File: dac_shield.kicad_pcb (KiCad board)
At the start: 2 copper layers, 68.6 x 53.3 mm, 32 parts, among them P1 V+, P2 GND, P3 V-, P4 Out, P5 GND, U1 LM741, U2 TCA0372

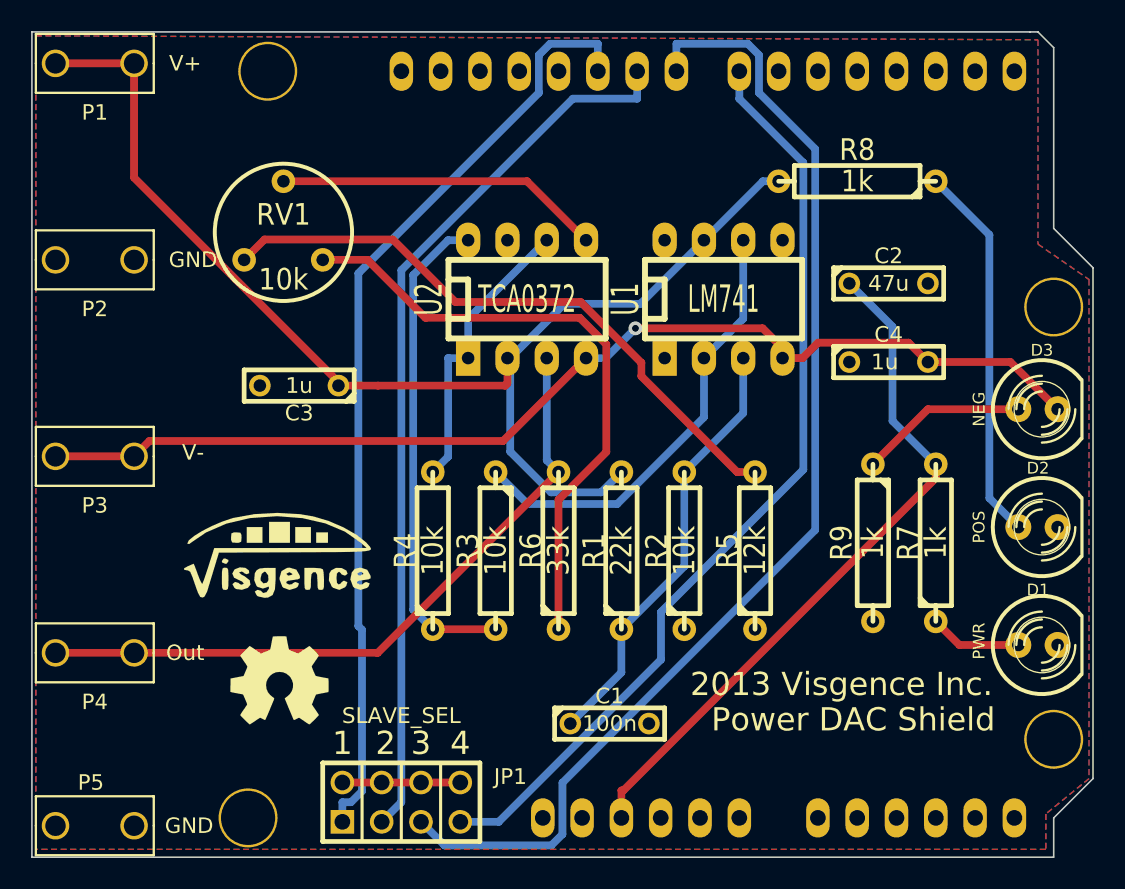
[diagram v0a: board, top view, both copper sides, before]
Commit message: Added DAC back on board
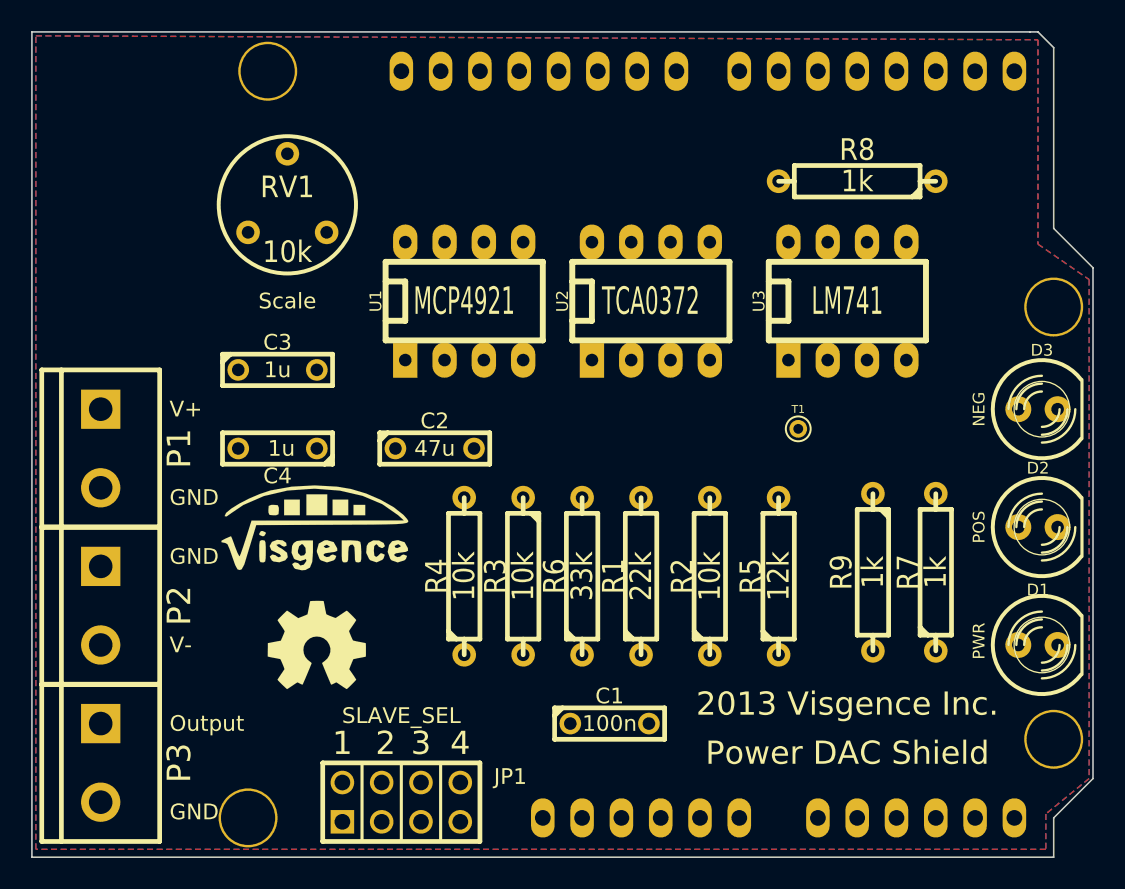
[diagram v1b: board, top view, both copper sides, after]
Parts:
- removed P4: Out, Johnson_Banana
- removed P5: GND, Johnson_Banana
- added T1: VrefTest, PINTST, F.Cu at (80.0, 54.6)
- added U3: LM741, DIP-8__300_ELL, F.Cu at (83.2, 46.4)
- P1: value V+ -> CONN_2; footprint Johnson_Banana -> bornier2
- P2: value GND -> CONN_2; footprint Johnson_Banana -> bornier2
- P3: value V- -> CONN_2; footprint Johnson_Banana -> bornier2
- U1: value LM741 -> MCP4921
- moved C4 39.9 mm to (46.4, 55.9), turned to 180 degrees
- moved C2 31.2 mm to (56.5, 55.9)
- moved P1 24.9 mm to (34.9, 55.9), turned to 270 degrees
- moved P2 22.4 mm to (34.9, 66.0), turned to 270 degrees
- moved P3 19.8 mm to (34.9, 76.2), turned to 270 degrees
- moved U1 16.8 mm to (58.4, 46.4)
- moved U2 8.00 mm to (70.5, 46.4)
- moved G2 3.32 mm to (48.9, 68.6)
- moved G1 3.00 mm to (48.9, 61.0)
- moved R4 2.62 mm to (58.4, 64.1)
- moved R3 2.43 mm to (62.2, 64.1)
- moved R2 2.33 mm to (74.3, 64.1)
- moved R5 2.25 mm to (78.7, 64.1)
- moved R6 2.25 mm to (66.0, 64.1)
- moved R1 2.08 mm to (69.8, 64.1)
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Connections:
- C1 pad 1: N-000005 (its old number) -> N-000007
- JP1 pad 2: N-000032 -> N-000037
- JP1 pad 4: N-000032 -> N-000037
- JP1 pad 6: N-000032 -> N-000037
- JP1 pad 8: N-000032 -> N-000037
- P3 pad 1: VSS -> N-000009
- R1 pad 1: N-000005 (its old number) -> N-000007
- R2 pad 2: N-000005 (its old number) -> N-000007
- R6 pad 2: N-000008 -> N-000009
- U1 pad 1: (no net) -> +5V
- U1 pad 2: VREF -> N-000037
- U1 pad 3: N-000005 (its old number) -> CLK
- U1 pad 4: VSS -> MOSI
- U1 pad 5: (no net) -> GND
- U1 pad 7: VDD -> GND
- U1 pad 8: (no net) -> DAC_OUT
- U2 pad 3: N-000008 -> N-000009
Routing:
- net VDD: track 81.0 -> 0.00 mm
- net N-000035: track 76.1 -> 0.00 mm
- net VSS: track 71.8 -> 0.00 mm, vias 1 -> 0
- net N-000036: track 61.2 -> 0.00 mm
- net N-000034: track 60.9 -> 0.00 mm
- net N-000033: track 57.8 -> 0.00 mm
- net +5V: track 45.4 -> 0.00 mm
- net N-000008: track 45.0 -> 0.00 mm
- net N-000039: track 40.3 -> 0.00 mm
- net N-000040: track 40.3 -> 0.00 mm
- net N-000041: track 32.0 -> 0.00 mm
- net VREF: track 29.1 -> 0.00 mm
- net N-000005 (its old number): track 28.3 -> 0.00 mm
- net N-000003: track 24.6 -> 0.00 mm
- net N-000043: track 21.1 -> 0.00 mm
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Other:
- board text added: "GND"
- board text added: "Output"
- board text added: "Scale"
- board text added: "V+"
- board text added: "V-"

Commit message: Added pinouts on silk screen
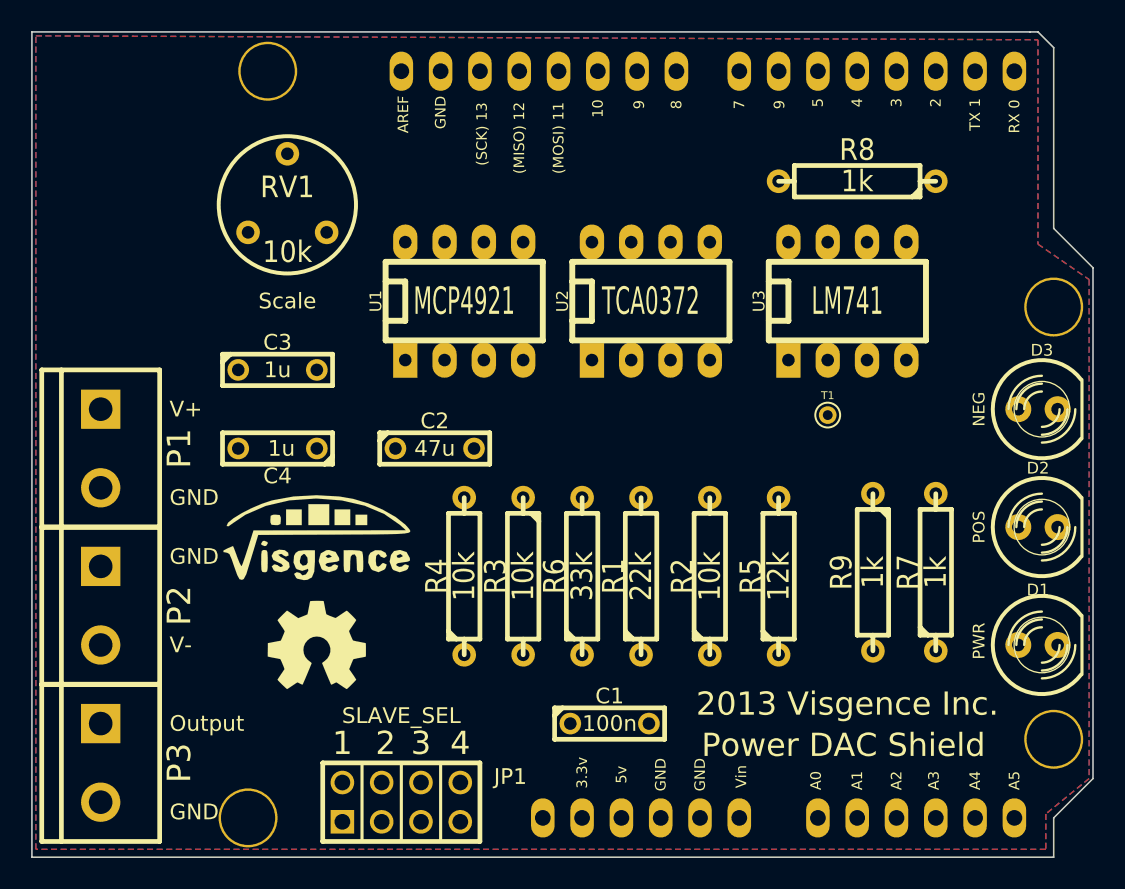
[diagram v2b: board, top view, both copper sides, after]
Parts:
- moved T1 2.10 mm to (81.9, 53.7)
- moved G1 0.65 mm to (49.0, 61.6)
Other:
- board text added: "(MISO) 12"
- board text added: "(MOSI) 11"
- board text added: "(SCK) 13"
- board text added: "10"
- board text added: "3.3v"
- board text added: "5"
- board text added: "5v"
- board text added: "6"
- board text added: "7"
- board text added: "8"
- board text added: "9"
- board text added: "A0"
- board text added: "A1"
- board text added: "A2"
- board text added: "A3"
- board text added: "A4"
- board text added: "A5"
- board text added: "AREF"
- board text added: "RX 0"
- board text added: "TX 1"
- board text added: "Vin"
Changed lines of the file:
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@@
     (area 30.429999 28.905999 99.110001 82.346001)
     (thickness 1.6)
-    (drawings 26)
+    (drawings 53)
     (tracks 0)
     (zones 0)
@@
     (trace_min 0.254)
     (segment_width 0.2)
-    (edge_width 0.1)
+    (edge_width 0.127)
     (via_size 0.889)
     (via_drill 0.635)
@@
     (uvia_min_size 0.508)
     (uvia_min_drill 0.127)
-    (pcb_text_width 0.3)
-    (pcb_text_size 1.016 1.016)
+    (pcb_text_width 0.127)
+    (pcb_text_size 0.6858 0.6858)
     (mod_edge_width 0.15)
     (mod_text_size 1 1)
@@
   )
   (module LOGO (layer F.Cu)
-    (at 48.895 60.96)
+    (at 49.022 61.595)
     (fp_text reference G1 (at 0 3.63982) (layer F.SilkS) hide
       (effects (font (size 1.524 1.524) (thickness 0.3048)))
@@
   )
   (module PINTST (layer F.Cu)
-    (at 80.01 54.61)
+    (at 81.915 53.721)
     (descr "module 1 pin (ou trou mecanique de percage)")
     (tags DEV)
@@
     )
   )
+  (gr_text A5 (at 93.98 77.343 90) (layer F.SilkS)
+    (effects (font (size 0.6858 0.6858) (thickness 0.127)))
+  )
+  (gr_text A4 (at 91.44 77.343 90) (layer F.SilkS)
+    (effects (font (size 0.6858 0.6858) (thickness 0.127)))
+  )
+  (gr_text A3 (at 88.773 77.343 90) (layer F.SilkS)
+    (effects (font (size 0.6858 0.6858) (thickness 0.127)))
+  )
+  (gr_text A2 (at 86.36 77.343 90) (layer F.SilkS)
+    (effects (font (size 0.6858 0.6858) (thickness 0.127)))
+  )
+  (gr_text A1 (at 83.82 77.343 90) (layer F.SilkS)
+    (effects (font (size 0.6858 0.6858) (thickness 0.127)))
+  )
+  (gr_text A0 (at 81.153 77.343 90) (layer F.SilkS)
+    (effects (font (size 0.6858 0.6858) (thickness 0.127)))
+  )
+  (gr_text Vin (at 76.327 77.089 90) (layer F.SilkS)
+    (effects (font (size 0.6858 0.6858) (thickness 0.127)))
+  )
+  (gr_text GND (at 73.66 76.962 90) (layer F.SilkS)
+    (effects (font (size 0.6858 0.6858) (thickness 0.127)))
+  )
+  (gr_text GND (at 71.12 76.962 90) (layer F.SilkS)
+    (effects (font (size 0.6858 0.6858) (thickness 0.127)))
+  )
+  (gr_text 5v (at 68.58 76.962 90) (layer F.SilkS)
+    (effects (font (size 0.6858 0.6858) (thickness 0.127)))
+  )
+  (gr_text 3.3v (at 66.04 76.835 90) (layer F.SilkS)
+    (effects (font (size 0.6858 0.6858) (thickness 0.127)))
+  )
+  (gr_text "RX 0" (at 93.98 34.417 90) (layer F.SilkS)
+    (effects (font (size 0.6858 0.6858) (thickness 0.127)))
+  )
+  (gr_text "TX 1" (at 91.44 34.29 90) (layer F.SilkS)
+    (effects (font (size 0.6858 0.6858) (thickness 0.127)))
+  )
+  (gr_text 2 (at 88.9 33.528 90) (layer F.SilkS)
+    (effects (font (size 0.6858 0.6858) (thickness 0.127)))
+  )
+  (gr_text 3 (at 86.36 33.528 90) (layer F.SilkS)
+    (effects (font (size 0.6858 0.6858) (thickness 0.127)))
+  )
+  (gr_text 4 (at 83.82 33.528 90) (layer F.SilkS)
+    (effects (font (size 0.6858 0.6858) (thickness 0.127)))
+  )
+  (gr_text 5 (at 81.28 33.528 90) (layer F.SilkS)
+    (effects (font (size 0.6858 0.6858) (thickness 0.127)))
+  )
+  (gr_text 6 (at 78.74 33.655 270) (layer F.SilkS)
+    (effects (font (size 0.6858 0.6858) (thickness 0.127)))
+  )
+  (gr_text 7 (at 76.2 33.655 90) (layer F.SilkS)
+    (effects (font (size 0.6858 0.6858) (thickness 0.127)))
+  )
+  (gr_text 8 (at 72.136 33.655 90) (layer F.SilkS)
+    (effects (font (size 0.6858 0.6858) (thickness 0.127)))
+  )
+  (gr_text 9 (at 69.723 33.655 90) (layer F.SilkS)
+    (effects (font (size 0.6858 0.6858) (thickness 0.127)))
+  )
+  (gr_text 10 (at 67.056 33.909 90) (layer F.SilkS)
+    (effects (font (size 0.6858 0.6858) (thickness 0.127)))
+  )
+  (gr_text "(MOSI) 11" (at 64.516 35.814 90) (layer F.SilkS)
+    (effects (font (size 0.6858 0.6858) (thickness 0.127)))
+  )
+  (gr_text "(MISO) 12" (at 61.976 35.814 90) (layer F.SilkS)
+    (effects (font (size 0.6858 0.6858) (thickness 0.127)))
+  )
+  (gr_text "(SCK) 13" (at 59.563 35.56 90) (layer F.SilkS)
+    (effects (font (size 0.6858 0.6858) (thickness 0.127)))
+  )
+  (gr_text AREF (at 54.483 34.29 90) (layer F.SilkS)
+    (effects (font (size 0.6858 0.6858) (thickness 0.127)))
+  )
+  (gr_text GND (at 56.896 34.163 90) (layer F.SilkS)
+    (effects (font (size 0.6858 0.6858) (thickness 0.127)))
+  )
   (gr_text Scale (at 46.99 46.355) (layer F.SilkS)
     (effects (font (size 1.016 1.016) (thickness 0.254)))
@@
     (effects (font (size 1.5 1.5) (thickness 0.3)))
   )
-  (gr_text "Power DAC Shield" (at 83.185 75.565) (layer F.SilkS)
+  (gr_text "Power DAC Shield" (at 82.931 75.057) (layer F.SilkS)
     (effects (font (size 1.5 1.5) (thickness 0.3)))
   )

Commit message: Did first try at routing
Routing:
- net N-000035: track 0.00 -> 93.6 mm
- net N-000034: track 0.00 -> 92.1 mm
- net VSS: track 0.00 -> 74.6 mm
- net VDD: track 0.00 -> 66.6 mm
- net N-000036: track 0.00 -> 65.1 mm
- net N-000040: track 0.00 -> 64.4 mm
- net +5V: track 0.00 -> 63.0 mm
- net N-000033: track 0.00 -> 61.0 mm, vias 0 -> 1
- net N-000009: track 0.00 -> 52.8 mm
- net VREF: track 0.00 -> 49.7 mm, vias 0 -> 1
- net N-000039: track 0.00 -> 45.3 mm
- net N-000037: track 0.00 -> 34.8 mm
- net N-000007: track 0.00 -> 33.8 mm
- net N-000041: track 0.00 -> 32.3 mm
- net N-000043: track 0.00 -> 29.7 mm
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
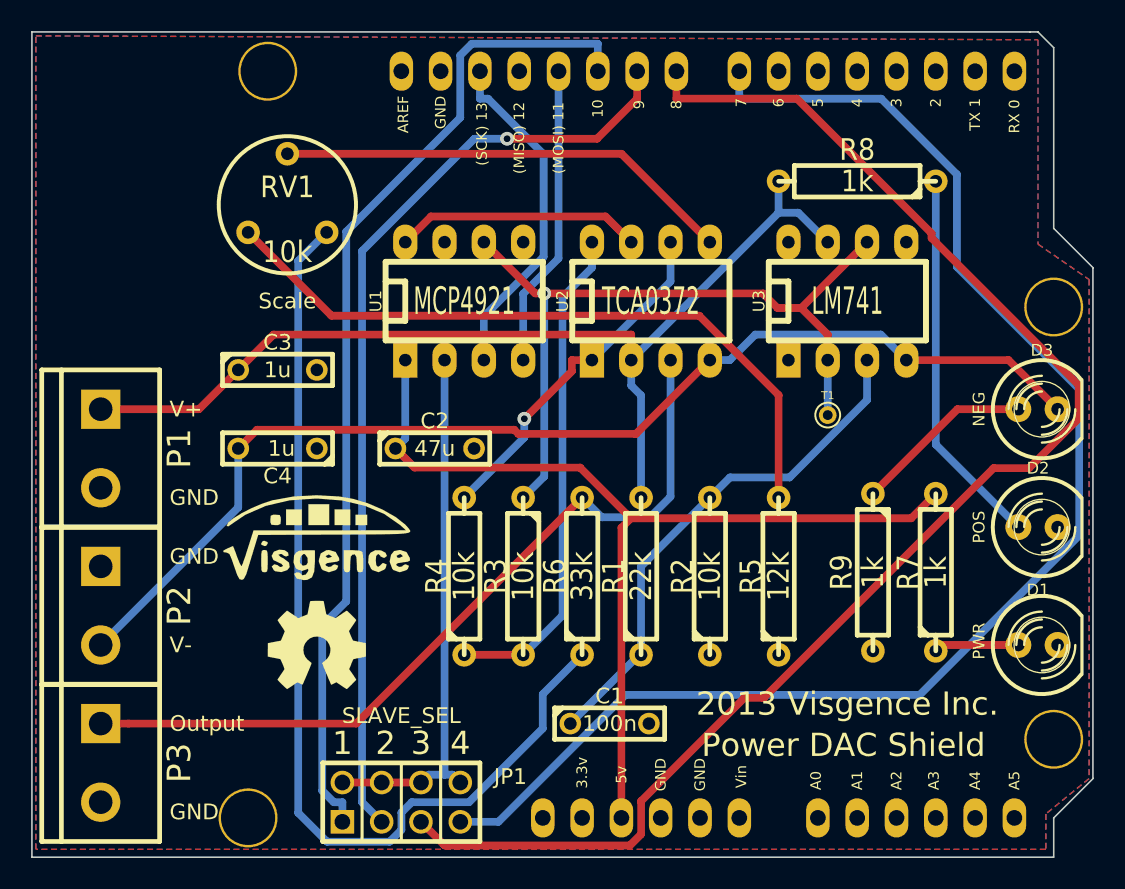
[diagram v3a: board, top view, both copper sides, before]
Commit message: Had to move chip for more room, rerouted
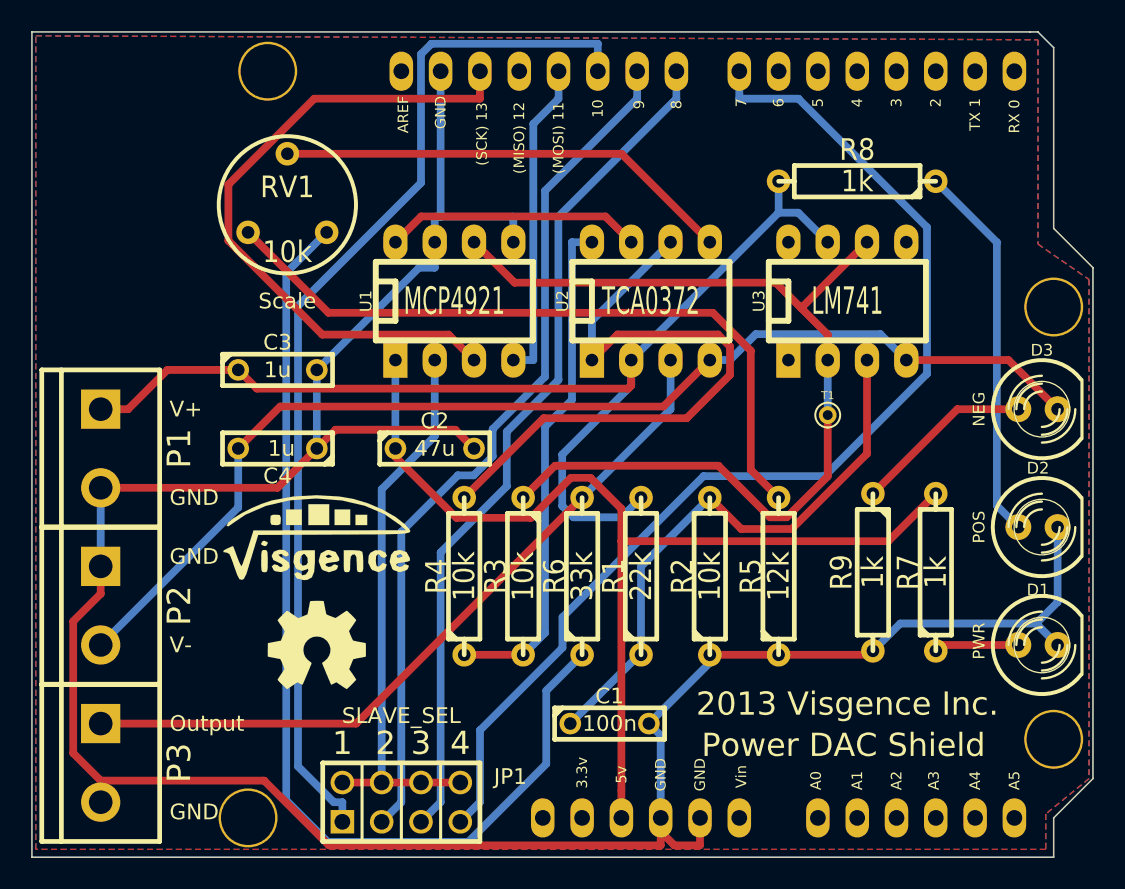
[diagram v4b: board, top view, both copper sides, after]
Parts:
- moved U1 0.64 mm to (57.8, 46.4)
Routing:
- net GND: track 0.00 -> 170.4 mm
- net N-000035: track 93.6 -> 55.4 mm
- net CLK: track 22.3 -> 43.0 mm
- net N-000034: track 92.1 -> 72.9 mm
- net N-000042: track 22.8 -> 42.0 mm, vias 1 -> 0
- net VREF: track 49.7 -> 63.5 mm, vias 1 -> 0
- net VDD: track 66.6 -> 74.2 mm
- net N-000033: track 61.0 -> 55.9 mm, vias 1 -> 0
- net N-000009: track 52.8 -> 48.4 mm
- net N-000007: track 33.8 -> 37.5 mm
- net +5V: track 63.0 -> 66.0 mm
- net N-000036: track 65.1 -> 67.9 mm
- net N-000037: track 34.8 -> 36.3 mm
- net N-000040: track 64.4 -> 65.8 mm
- net MOSI: track 19.6 -> 20.6 mm
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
